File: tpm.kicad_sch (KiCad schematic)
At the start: 6 parts, among them J801 PinHeader_2x7_P2mm_MTMM-107-0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, U801 TS3A27518E_QFN

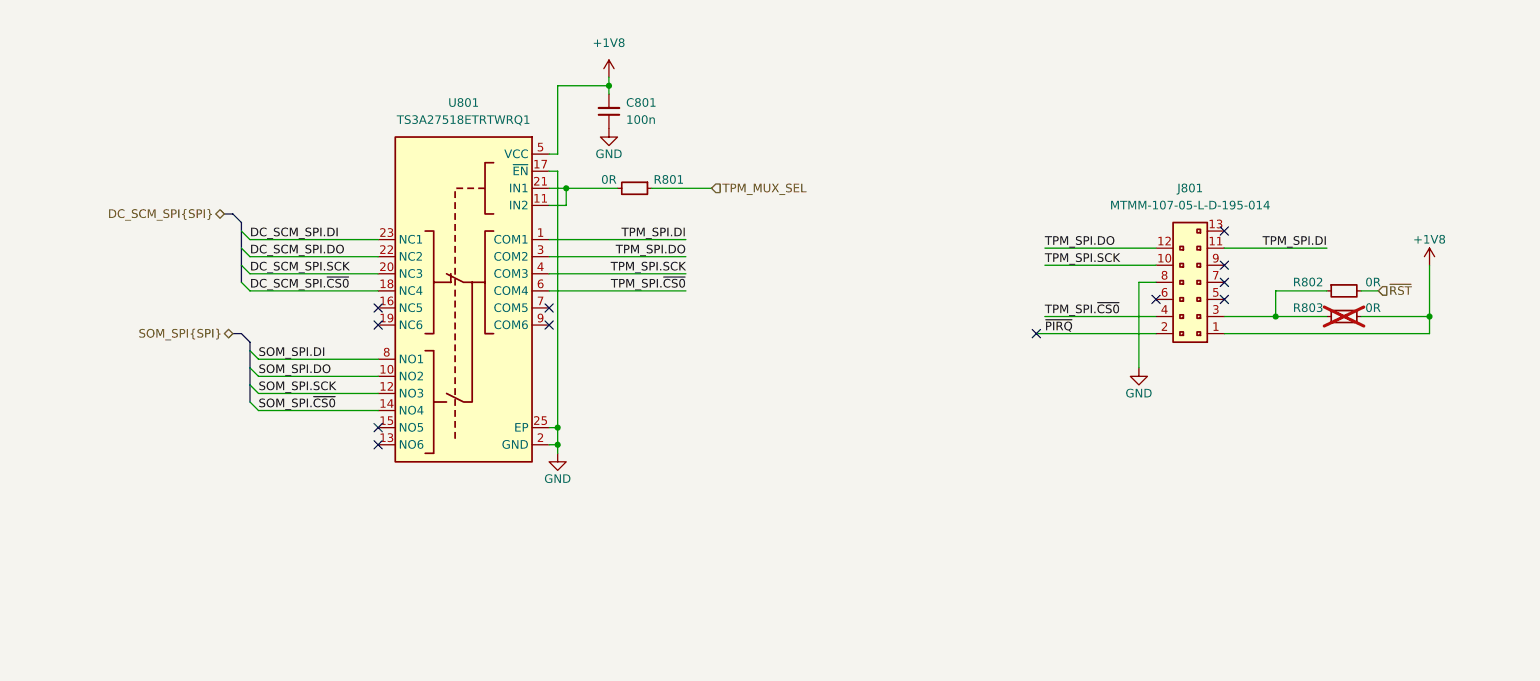
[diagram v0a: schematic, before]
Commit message: [#99732] Fix TMP connection - connect via MUX to SPI and QSPI from DC-SCM
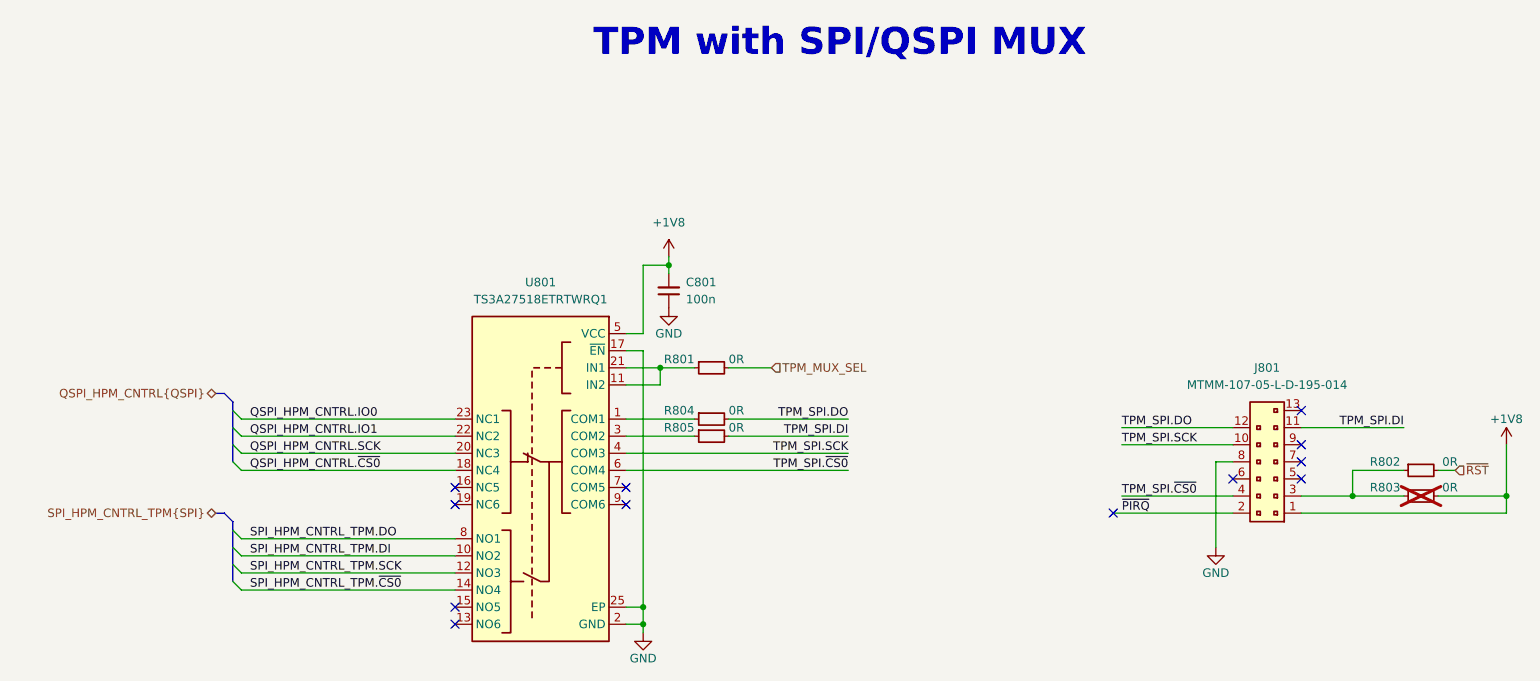
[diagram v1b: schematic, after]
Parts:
- added R804, R805: R_0R_0402, antmicro-footprints:R_0402_1005Metric, symbol antmicroResistors0402:R_0R_0402
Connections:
- net TPM_MUX_SEL: now also R801.2; no longer R801.1
- net TPM_SPI.DI: now also R805.2; no longer U801.1 (COM1)
- net TPM_SPI.DO: now also R804.2; no longer U801.3 (COM2)
- net at U801.11 (IN2), U801.21 (IN1): now also R801.1; no longer R801.2
- net DC_SCM_SPI.DI renamed QSPI_HPM_CNTRL.IO0
- net DC_SCM_SPI.DO renamed QSPI_HPM_CNTRL.IO1
- net DC_SCM_SPI.SCK renamed QSPI_HPM_CNTRL.SCK
- net DC_SCM_SPI.~{CS0} renamed QSPI_HPM_CNTRL.~{CS0}
- net SOM_SPI.DI renamed SPI_HPM_CNTRL_TPM.DO
- net SOM_SPI.DO renamed SPI_HPM_CNTRL_TPM.DI
- net SOM_SPI.SCK renamed SPI_HPM_CNTRL_TPM.SCK
- net SOM_SPI.~{CS0} renamed SPI_HPM_CNTRL_TPM.~{CS0}
- new net: R804.1, U801.1 (COM1)
- new net: R805.1, U801.3 (COM2)
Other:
- note added: "TPM with SPI/QSPI MUX"
- moved on the sheet: C801, J801, R802, R803, U801

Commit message: [#99781] Update mismatached component values
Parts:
- removed J801: PinHeader_2x7_P2mm_MTMM-107-05-L-D-195-014, antmicro-footprints:PinHeader_2x7_P2mm_Drill0.9mm_MTMM, symbol antmicroGenericPinHeaders:PinHeader_2x7_P2mm_MTMM-107-05-L-D-195-014
- added J801: PinHeader_2x7_P2mm_Drill0.9mm_MTMM-107-05-L-D-195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, antmicro-footprints:PinHeader_2x7_P2mm_Drill0.9mm_MTMM-107-05-L-D-195-014, symbol antmicroGenericPinHeaders:PinHeader_2x7_P2mm_Drill0.9mm_MTMM-107-05-L-D-195-014
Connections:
- net +1V8: now also J801.1
- net GND: now also J801.8
- net TPM_SPI.DI: now also J801.11
- net TPM_SPI.DO: now also J801.12
- net TPM_SPI.SCK: now also J801.10
- net TPM_SPI.~{CS0}: now also J801.4
- net ~{PIRQ}: now also J801.2
- net at R802.1, R803.1: now also J801.3
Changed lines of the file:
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@@
+	)
+	(symbol
+		(lib_id "antmicroGenericPinHeaders:PinHeader_2x7_P2mm_Drill0.9mm_MTMM-107-05-L-D-195-014")
+		(at 284.48 158.75 180)
+		(unit 1)
+		(body_style 1)
+		(exclude_from_sim no)
+		(in_bom yes)
+		(on_board yes)
+		(in_pos_files yes)
+		(dnp no)
+		(fields_autoplaced yes)
+		(property "Reference" "J801"
+			(at 279.4 137.16 0)
+			(show_name no)
+			(do_not_autoplace no)
+			(effects
+				(font
+					(size 1.27 1.27)
+					(thickness 0.15)
+				)
+			)
+		)
+		(property "Value" "PinHeader_2x7_P2mm_Drill0.9mm_MTMM-107-05-L-D-195-014"
+			(at 259.08 148.59 0)
+			(hide yes)
+			(show_name no)
+			(do_not_autoplace no)
+			(effects
+				(font
+					(size 1.27 1.27)
+					(thickness 0.15)
+				)
+				(justify left bottom)
+			)
+		)
+		(property "Footprint" "antmicro-footprints:PinHeader_2x7_P2mm_Drill0.9mm_MTMM-107-05-L-D-195-014"
+			(at 259.08 146.05 0)
+			(hide yes)
+			(show_name no)
+			(do_not_autoplace no)
+			(effects
+				(font
+					(size 1.27 1.27)
+					(thickness 0.15)
+				)
+				(justify left bottom)
+			)
+		)
+		(property "Datasheet" "https://suddendocs.samtec.com/catalog_english/mtmm_th.pdf"
+			(at 259.08 143.51 0)
+			(hide yes)
+			(show_name no)
+			(do_not_autoplace no)
+			(effects
+				(font
+					(size 1.27 1.27)
+					(thickness 0.15)
+				)
+				(justify left bottom)
+			)
+		)
+		(property "Description" "Pin Header, 2 Rows, 13 Contacts, 2.00mm"
+			(at 259.08 140.97 0)
+			(hide yes)
+			(show_name no)
+			(do_not_autoplace no)
+			(effects
+				(font
+					(size 1.27 1.27)
+					(thickness 0.15)
+				)
+				(justify left bottom)
+			)
+		)
+		(property "MPN" "MTMM-107-05-L-D-195-014"
+			(at 279.4 139.7 0)
+			(show_name no)
+			(do_not_autoplace no)
+			(effects
+				(font
+					(size 1.27 1.27)
+					(thickness 0.15)
+				)
+			)
+		)
+		(property "Manufacturer" "Samtec"
+			(at 259.08 138.43 0)
+			(hide yes)
+			(show_name no)
+			(do_not_autoplace no)
+			(effects
+				(font
+					(size 1.27 1.27)
+					(thickness 0.15)
+				)
+				(justify left bottom)
+			)
+		)
+		(property "Author" "Antmicro"
+			(at 259.08 135.89 0)
+			(hide yes)
+			(show_name no)
+			(do_not_autoplace no)
+			(effects
+				(font
+					(size 1.27 1.27)
+					(thickness 0.15)
+				)
+				(justify left bottom)
+			)
+		)
+		(property "License" "Apache-2.0"
+			(at 259.08 133.35 0)
+			(hide yes)
+			(show_name no)
+			(do_not_autoplace no)
+			(effects
+				(font
+					(size 1.27 1.27)
+					(thickness 0.15)
+				)
+				(justify left bottom)
+			)
+		)
+		(pin "13"
+		)
+		(pin "11"
+		)
+		(pin "10"
+		)
+		(pin "9"
+		)
+		(pin "3"
+		)
+		(pin "12"
+		)
+		(pin "7"
+		)
+		(pin "6"
+		)
+		(pin "8"
+		)
+		(pin "5"
+		)
+		(pin "4"
+		)
+		(pin "1"
+		)
+		(pin "2"
+		)
+		(instances
+			(project "altera-modular-agilex-5-dc-scm"
+				(path "/6bb9d978-a328-4b30-874b-55170a976185/af45e011-8332-484c-9b46-08bd6b2c8877"
+					(reference "J801")
+					(unit 1)
+				)
+			)
+		)
 	)
 	(symbol
@@
 					(unit 1)
 				)
-			)
-		)
-	)
-	(symbol
-		(lib_id "antmicroGenericPinHeaders:PinHeader_2x7_P2mm_MTMM-107-05-L-D-195-014")
-		(at 284.48 158.75 180)
-		(unit 1)
-		(body_style 1)
-		(exclude_from_sim no)
-		(in_bom yes)
-		(on_board yes)
-		(in_pos_files yes)
-		(dnp no)
-		(fields_autoplaced yes)
-		(property "Reference" "J801"
-			(at 279.4 137.16 0)
-			(show_name no)
-			(do_not_autoplace no)
-			(effects
-				(font
-					(size 1.27 1.27)
-					(thickness 0.15)
-				)
-			)
-		)
-		(property "Value" "PinHeader_2x7_P2mm_MTMM-107-05-L-D-195-014"
-			(at 259.08 148.59 0)
-			(hide yes)
-			(show_name no)
-			(do_not_autoplace no)
-			(effects
-				(font
-					(size 1.27 1.27)
-					(thickness 0.15)
-				)
-				(justify left bottom)
-			)
-		)
-		(property "Footprint" "antmicro-footprints:PinHeader_2x7_P2mm_Drill0.9mm_MTMM"
-			(at 259.08 146.05 0)
-			(hide yes)
-			(show_name no)
-			(do_not_autoplace no)
-			(effects
-				(font
-					(size 1.27 1.27)
-					(thickness 0.15)
-				)
-				(justify left bottom)
-			)
-		)
-		(property "Datasheet" "https://suddendocs.samtec.com/catalog_english/mtmm_th.pdf"
-			(at 259.08 143.51 0)
-			(hide yes)
-			(show_name no)
-			(do_not_autoplace no)
-			(effects
-				(font
-					(size 1.27 1.27)
-					(thickness 0.15)
-				)
-				(justify left bottom)
-			)
-		)
-		(property "Description" "Pin Header, 2 Rows, 13 Contacts, 2.00mm"
-			(at 259.08 140.97 0)
-			(hide yes)
-			(show_name no)
-			(do_not_autoplace no)
-			(effects
-				(font
-					(size 1.27 1.27)
-					(thickness 0.15)
-				)
-				(justify left bottom)
-			)
-		)
-		(property "MPN" "MTMM-107-05-L-D-195-014"
-			(at 279.4 139.7 0)
-			(show_name no)
-			(do_not_autoplace no)
-			(effects
-				(font
-					(size 1.27 1.27)
-					(thickness 0.15)
-				)
-			)
-		)
-		(property "Manufacturer" "Samtec"
-			(at 259.08 138.43 0)
-			(hide yes)
-			(show_name no)
-			(do_not_autoplace no)
-			(effects
-				(font
-					(size 1.27 1.27)
-					(thickness 0.15)
-				)
-				(justify left bottom)
-			)
-		)
-		(property "Author" "Antmicro"
-			(at 259.08 135.89 0)
-			(hide yes)
-			(show_name no)
-			(do_not_autoplace no)
-			(effects
-				(font
-					(size 1.27 1.27)
-					(thickness 0.15)
-				)
-				(justify left bottom)
-			)
-		)
-		(property "License" "Apache-2.0"
-			(at 259.08 133.35 0)
-			(hide yes)
-			(show_name no)
-			(do_not_autoplace no)
-			(effects
-				(font
-					(size 1.27 1.27)
-					(thickness 0.15)
-				)
-				(justify left bottom)
-			)
-		)
-		(pin "9"
-		)
-		(pin "7"
-		)
-		(pin "8"
-		)
-		(pin "2"
-		)
-		(pin "11"
-		)
-		(pin "1"
-		)
-		(pin "3"
-		)
-		(pin "13"
-		)
-		(pin "5"
-		)
-		(pin "12"
-		)
-		(pin "4"
-		)
-		(pin "6"
-		)
-		(pin "10"
-		)
-		(instances
-			(project "altera-modular-agilex-5-dc-scm"
-				(path "/6bb9d978-a328-4b30-874b-55170a976185/af45e011-8332-484c-9b46-08bd6b2c8877"
-					(reference "J801")
-					(unit 1)
-				)

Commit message: [#100282] Reorder schematic pages, reannotate schematic
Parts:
- renumbered C801 to C1001, J801 to J1001, R801 to R1001, R804 to R1002, R805 to R1003, R802 to R1004, R803 to R1005, U801 to U1001
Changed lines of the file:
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@@
 		(in_pos_files yes)
 		(dnp no)
-		(property "Reference" "#PWR0805"
+		(property "Reference" "#PWR01003"
 			(at 330.2 151.13 0)
 			(hide yes)
@@
 			(project "altera-modular-agilex-5-dc-scm"
 				(path "/6bb9d978-a328-4b30-874b-55170a976185/af45e011-8332-484c-9b46-08bd6b2c8877"
-					(reference "#PWR0805")
+					(reference "#PWR01003")
 					(unit 1)
 				)
@@
 		(dnp no)
 		(fields_autoplaced yes)
-		(property "Reference" "J801"
+		(property "Reference" "J1001"
 			(at 279.4 137.16 0)
 			(show_name no)
@@
 			(project "altera-modular-agilex-5-dc-scm"
 				(path "/6bb9d978-a328-4b30-874b-55170a976185/af45e011-8332-484c-9b46-08bd6b2c8877"
-					(reference "J801")
+					(reference "J1001")
 					(unit 1)
 				)
@@
 		(in_pos_files yes)
 		(dnp no)
-		(property "Reference" "#PWR0801"
+		(property "Reference" "#PWR01005"
 			(at 177.8 179.07 0)
 			(hide yes)
@@
 			(project "altera-modular-agilex-5-dc-scm"
 				(path "/6bb9d978-a328-4b30-874b-55170a976185/af45e011-8332-484c-9b46-08bd6b2c8877"
-					(reference "#PWR0801")
+					(reference "#PWR01005")
 					(unit 1)
 				)
@@
 		(in_pos_files yes)
 		(dnp no)
-		(property "Reference" "R804"
+		(property "Reference" "R1002"
 			(at 194.31 143.51 0)
 			(show_name no)
@@
 			(project "altera-modular-agilex-5-dc-scm"
 				(path "/6bb9d978-a328-4b30-874b-55170a976185/af45e011-8332-484c-9b46-08bd6b2c8877"
-					(reference "R804")
+					(reference "R1002")
 					(unit 1)
 				)
@@
 		(in_pos_files yes)
 		(dnp no)
-		(property "Reference" "U801"
+		(property "Reference" "U1001"
 			(at 171.45 124.46 0)
 			(show_name no)
@@
 			(project "altera-modular-agilex-5-dc-scm"
 				(path "/6bb9d978-a328-4b30-874b-55170a976185/af45e011-8332-484c-9b46-08bd6b2c8877"
-					(reference "U801")
+					(reference "U1001")
 					(unit 1)
 				)
@@
 		(dnp no)
 		(fields_autoplaced yes)
-		(property "Reference" "C801"
+		(property "Reference" "C1001"
 			(at 193.04 124.4536 90)
 			(show_name no)
@@
 			(project "altera-modular-agilex-5-dc-scm"
 				(path "/6bb9d978-a328-4b30-874b-55170a976185/af45e011-8332-484c-9b46-08bd6b2c8877"
-					(reference "C801")
+					(reference "C1001")
 					(unit 1)
 				)
@@
 		(in_pos_files yes)
 		(dnp no)
-		(property "Reference" "R801"
+		(property "Reference" "R1001"
 			(at 194.31 135.89 0)
 			(show_name no)
@@
 			(project "altera-modular-agilex-5-dc-scm"
 				(path "/6bb9d978-a328-4b30-874b-55170a976185/af45e011-8332-484c-9b46-08bd6b2c8877"
-					(reference "R801")
+					(reference "R1001")
 					(unit 1)
 				)
@@
 		(in_pos_files yes)
 		(dnp no)
-		(property "Reference" "R802"
+		(property "Reference" "R1004"
 			(at 296.926 151.13 0)
 			(show_name no)
@@
 			(project "altera-modular-agilex-5-dc-scm"
 				(path "/6bb9d978-a328-4b30-874b-55170a976185/af45e011-8332-484c-9b46-08bd6b2c8877"
-					(reference "R802")
+					(reference "R1004")
 					(unit 1)
 				)
@@
 		(in_pos_files yes)
 		(dnp yes)
-		(property "Reference" "R803"
+		(property "Reference" "R1005"
 			(at 296.926 154.94 0)
 			(show_name no)
@@
 			(project "altera-modular-agilex-5-dc-scm"
 				(path "/6bb9d978-a328-4b30-874b-55170a976185/af45e011-8332-484c-9b46-08bd6b2c8877"
-					(reference "R803")
+					(reference "R1005")
 					(unit 1)
 				)
@@
 		(in_pos_files yes)
 		(dnp no)
-		(property "Reference" "R805"
+		(property "Reference" "R1003"
 			(at 194.31 146.05 0)
 			(show_name no)
@@
 			(project "altera-modular-agilex-5-dc-scm"
 				(path "/6bb9d978-a328-4b30-874b-55170a976185/af45e011-8332-484c-9b46-08bd6b2c8877"
-					(reference "R805")
+					(reference "R1003")
 					(unit 1)
 				)
@@
 		(dnp no)
 		(fields_autoplaced yes)
-		(property "Reference" "#PWR0802"
+		(property "Reference" "#PWR01001"
 			(at 205.74 123.19 0)
 			(hide yes)
@@
 			(project "altera-modular-agilex-5-dc-scm"
 				(path "/6bb9d978-a328-4b30-874b-55170a976185/af45e011-8332-484c-9b46-08bd6b2c8877"
-					(reference "#PWR0802")
+					(reference "#PWR01001")
 					(unit 1)
 				)
@@
 		(in_pos_files yes)
 		(dnp no)
-		(property "Reference" "#PWR0803"
+		(property "Reference" "#PWR01002"
 			(at 181.61 130.81 0)
 			(hide yes)
@@
 			(project "altera-modular-agilex-5-dc-scm"
 				(path "/6bb9d978-a328-4b30-874b-55170a976185/af45e011-8332-484c-9b46-08bd6b2c8877"
-					(reference "#PWR0803")
+					(reference "#PWR01002")
 					(unit 1)
 				)
@@
 		(in_pos_files yes)
 		(dnp no)
-		(property "Reference" "#PWR0804"
+		(property "Reference" "#PWR01004"
 			(at 280.67 166.37 0)
 			(hide yes)
@@
 			(project "altera-modular-agilex-5-dc-scm"
 				(path "/6bb9d978-a328-4b30-874b-55170a976185/af45e011-8332-484c-9b46-08bd6b2c8877"
-					(reference "#PWR0804")
+					(reference "#PWR01004")
 					(unit 1)
 				)

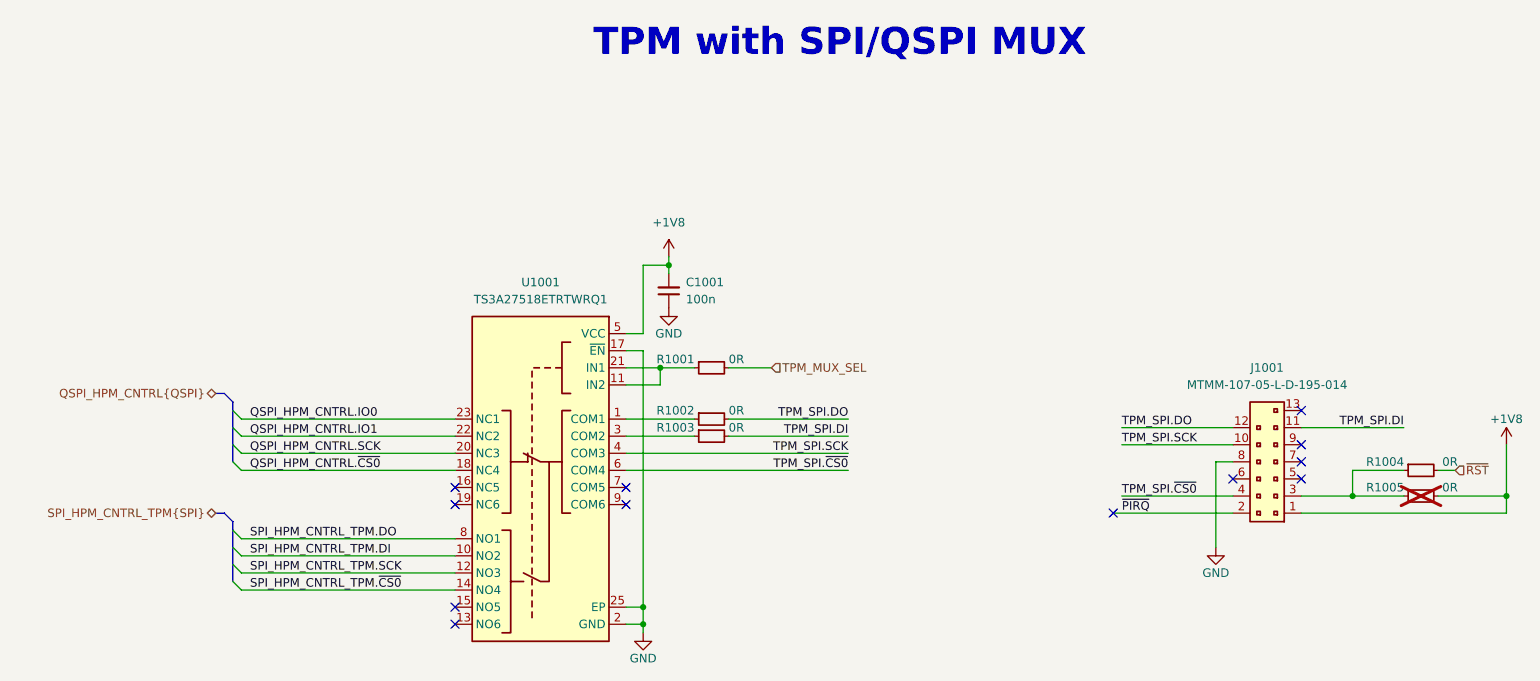
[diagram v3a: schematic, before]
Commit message: [#100282] Swap TMP default from QSPI to SPI, add level shifter for PECI I2C bus, connect user button
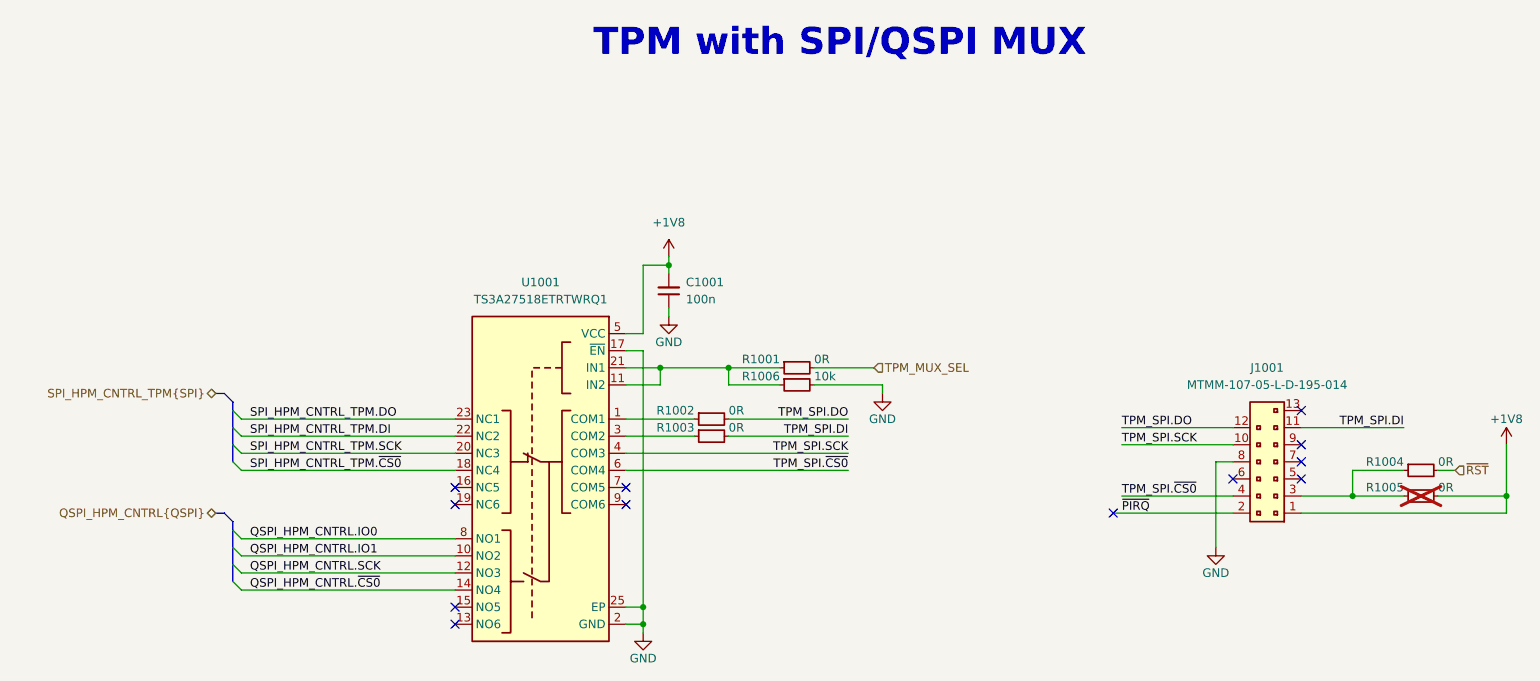
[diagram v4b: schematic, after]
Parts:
- added R1006: R_10k_0402, antmicro-footprints:R_0402_1005Metric, symbol antmicroResistors0402:R_10k_0402
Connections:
- net GND: now also R1006.2
- net QSPI_HPM_CNTRL.IO0: now also U1001.8 (NO1); no longer U1001.23 (NC1)
- net QSPI_HPM_CNTRL.IO1: now also U1001.10 (NO2); no longer U1001.22 (NC2)
- net QSPI_HPM_CNTRL.SCK: now also U1001.12 (NO3); no longer U1001.20 (NC3)
- net QSPI_HPM_CNTRL.~{CS0}: now also U1001.14 (NO4); no longer U1001.18 (NC4)
- net SPI_HPM_CNTRL_TPM.DI: now also U1001.22 (NC2); no longer U1001.10 (NO2)
- net SPI_HPM_CNTRL_TPM.DO: now also U1001.23 (NC1); no longer U1001.8 (NO1)
- net SPI_HPM_CNTRL_TPM.SCK: now also U1001.20 (NC3); no longer U1001.12 (NO3)
- net SPI_HPM_CNTRL_TPM.~{CS0}: now also U1001.18 (NC4); no longer U1001.14 (NO4)
- net at R1001.1, U1001.11 (IN2), U1001.21 (IN1): now also R1006.1
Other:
- moved on the sheet: R1001
